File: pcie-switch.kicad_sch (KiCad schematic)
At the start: 114 parts, among them Q2 BSS138PW,115, Q3 BSS138PW,115, Q7 BSS138PW,115, Q8 BSS138PW,115, Q9 BSS138PW,115, U1 PI7C9X3G606GP, U2 NTS0302JKZ

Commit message: [#100765] Apply fixes from review
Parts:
- removed D1, D2: LED_G_0603_LG_L29K-G2J1-24-Z, antmicro-footprints:LED_0603_1608Metric_G, symbol antmicroLEDIndicationDiscrete:LED_G_0603_LG_L29K-G2J1-24-Z
- removed R68: R_5k1_0402, antmicro-footprints:R_0402_1005Metric, symbol antmicroResistors0402:R_5k1_0402
- removed TP33: TP_1mm_SMD, antmicro-footprints:TP_SMD_1mm, symbol antmicroTestPoints:TP_1mm_SMD
- added C15, C16: C_4u7_25V_0402, antmicro-footprints:C_0402_1005Metric, symbol antmicroCapacitors0402:C_4u7_25V_0402
- added C41: C_100n_0402, antmicro-footprints:C_0402_1005Metric, symbol antmicroCapacitors0402:C_100n_0402
- added D1, D2: LED_Y_0402_VLMY1500-GS08, antmicro-footprints:LED_0402_1005Metric_Y, symbol antmicroLEDIndicationDiscrete:LED_Y_0402_VLMY1500-GS08
- added J1: Tag-Connect_TC2050-IDC-NL_2x5_P1.27mm, antmicro-footprints:Tag-Connect_TC2050-IDC-NL_2x5_P1.27mm, symbol antmicroTestPoints:Tag-Connect_TC2050-IDC-NL_2x5_P1.27mm
- added R111, R116: R_5k1_0402, antmicro-footprints:R_0402_1005Metric, symbol antmicroResistors0402:R_5k1_0402
- added R113, R114, R115, R27, R33: R_0R_0402, antmicro-footprints:R_0402_1005Metric, symbol antmicroResistors0402:R_0R_0402
- added R68: R_10k_0402, antmicro-footprints:R_0402_1005Metric, symbol antmicroResistors0402:R_10k_0402
- added TP26, TP27, TP28, TP29: TP_0.75mm_SMD, antmicro-footprints:TP_SMD_0.75mm, symbol antmicroTestPoints:TP_0.75mm_SMD
- added U12: 93AA66C_SOIC, antmicro-footprints:SOIC-8_3.9x4.9x1.75mm_P1.27mm, symbol antmicroMemory:93AA66C_SOIC
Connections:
- net +0V95: now also C15.2, C16.2
- net +1V8: now also C41.1, R111.1, R116.1, R68.2, U12.8 (VCC)
- net +3V3: now also D1.2 (A), D2.2 (A), R27.2
- net CS: now also R115.2, TP26.1, U12.1 (CS); no longer U1.M11 (~{EECS})
- net GND: now also C15.1, C16.1, C41.2, J1.3, J1.5, J1.9, U12.5 (GND)
- net MISO: now also R113.1, TP29.1, U12.4 (DO); no longer U1.J12 (EEDO)
- net MOSI: now also R114.2, TP28.1, U12.3 (DI); no longer U1.L11 (EEDI)
- net SCK: now also R33.1, TP27.1, U12.2 (CLK); no longer U1.K12 (EECK)
- net TCK: now also J1.4
- net TDI: now also J1.8
- net TDO: now also J1.6
- net TMS: now also J1.2
- net ~{RESET}: now also J1.10
- net at R21.2: now also D1.1 (C)
- net at R38.2: now also D2.1 (C)
- net at U1.L12 (SCL_I2C), U2.2 (A1): now also R111.2
- net at U1.M12 (SDA_I2C), U2.3 (A2): now also R116.2
- net ~{CLKREQ1}: no longer names the net of U1.E4 (~{CLKREQ1})
- new net: J1.1, R27.1
- new net: R114.1, U1.L11 (EEDI)
- new net: R68.1, U12.6 (ORG)
- new net: R113.2, U1.J12 (EEDO)
- new net: R115.1, U1.M11 (~{EECS})
- new net: R33.2, U1.K12 (EECK)
- no-connect marks 11 -> 12
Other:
- moved on the sheet: C10, C11, C12, C13, C14, C18, C2, C20, C21, C22, C26, C27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

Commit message: [#100765] Reset designators
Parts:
- renumbered C26 to C24, C5 to C25, C27 to C26, C2 to C27, C31 to C28, C6 to C29, C28 to C30, C3 to C31, C58 to C32, C29 to C33, C30 to C34, C32 to C35, C37 to C36, C33 to C37, C34 to C38, C64 to C39, C35 to C40, C7 to C41, C18 to C42, C38 to C43, C21 to C44, C36 to C45, C39 to C46, C8 to C47, C20 to C48, C22 to C49, C15 to C50, C4 to C51, C9 to C52, C10 to C53, C11 to C54, C12 to C55, C13 to C56, C14 to C57, C16 to C58, C41 to C59, D1 to D3, D2 to D4, D8 to D5, D9 to D6, D10 to D7, J1 to J5, Q2 to Q1, Q3 to Q2, Q7 to Q3, Q8 to Q4, Q9 to Q5, R33 to R32, R113 to R33, R21 to R34, R114 to R35, R115 to R36, R38 to R37, R7 to R38, R111 to R39, R5 to R40, R65 to R41, R116 to R42, R8 to R43, R25 to R44, R26 to R45, R6 to R46, R67 to R47, R19 to R48, R18 to R49, R100 to R50, R101 to R51, R98 to R52, R99 to R53, R1 to R54, R2 to R55, R39 to R56, R40 to R57, R45 to R58, R47 to R59, R46 to R60, R48 to R61, R41 to R62, R68 to R63, R82 to R64, R112 to R65, R11 to R66, R42 to R67, R43 to R68, R9 to R69, R10 to R70, R44 to R71, R36 to R72, R27 to R73, R34 to R74, R37 to R75, R35 to R76, R49 to R77, R85 to R78, R86 to R79, R28 to R80, R29 to R81, R50 to R82, R51 to R83, TP36 to TP19, TP37 to TP20, TP31 to TP21, TP24 to TP22, TP25 to TP23, TP26 to TP24, TP28 to TP25, TP27 to TP26, TP29 to TP27, TP40 to TP28, TP5 to TP29, TP12 to TP30, TP38 to TP31, TP39 to TP32, TP13 to TP33, TP14 to TP34, TP16 to TP35, TP6 to TP36, TP7 to TP37, TP8 to TP38, TP9 to TP39, TP10 to TP40, TP11 to TP41, TP17 to TP42, TP32 to TP43, TP34 to TP44, TP35 to TP45, U1 to U4, U2 to U5, U12 to U6

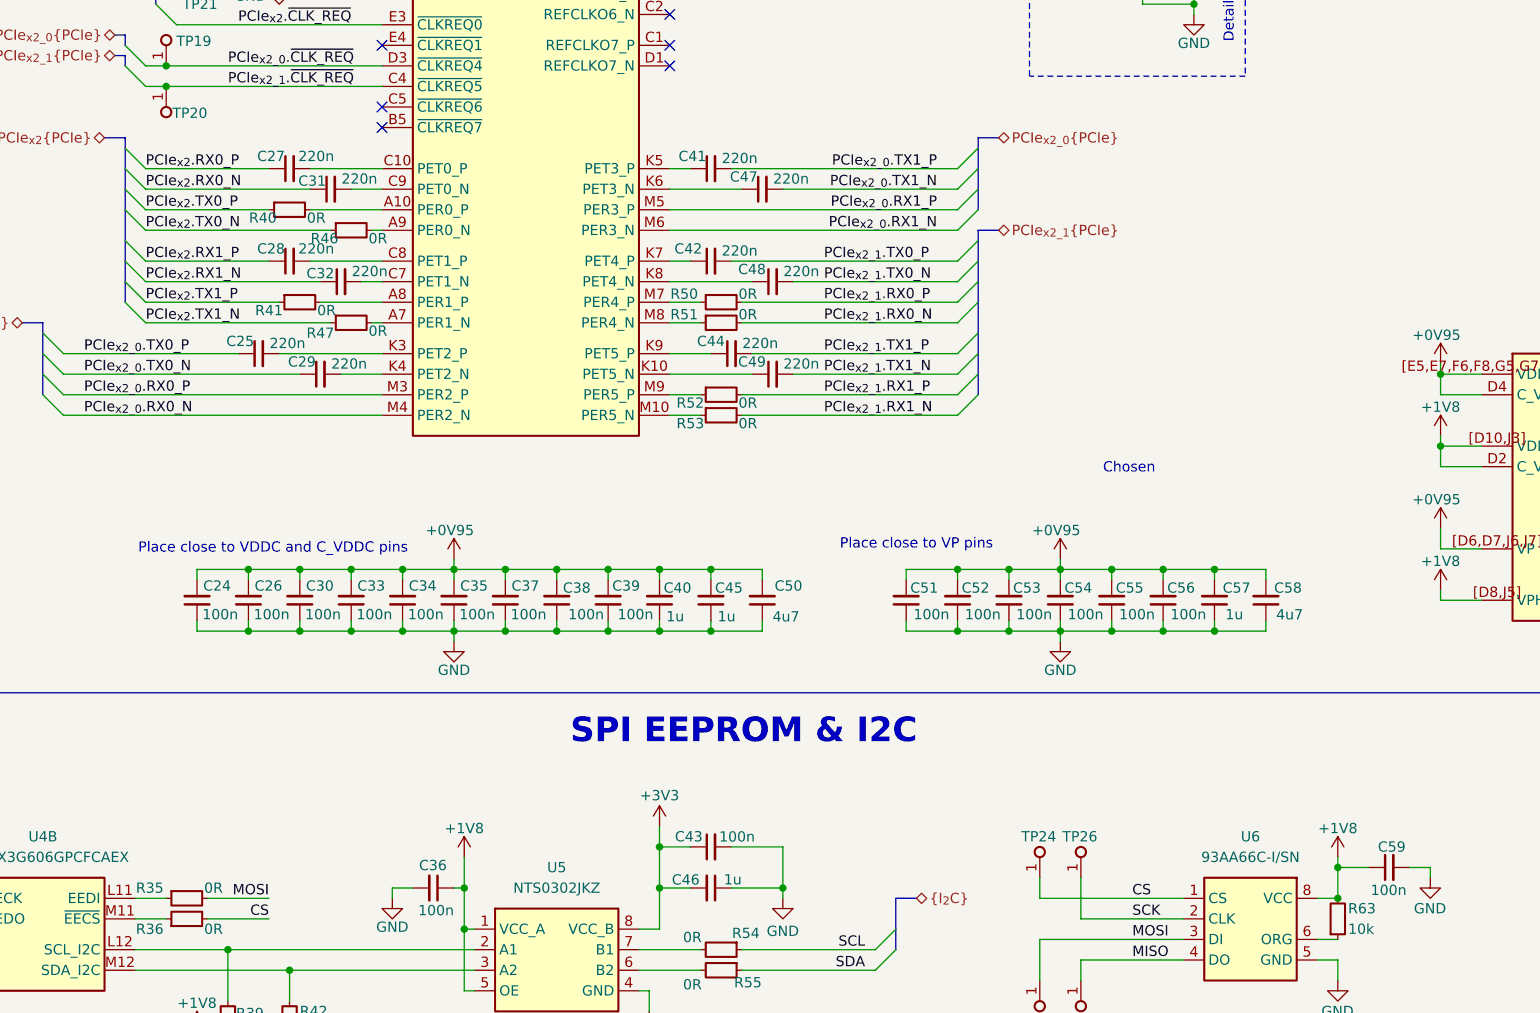
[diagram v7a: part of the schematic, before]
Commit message: [#101557] Add 0R on EEPROM VCC
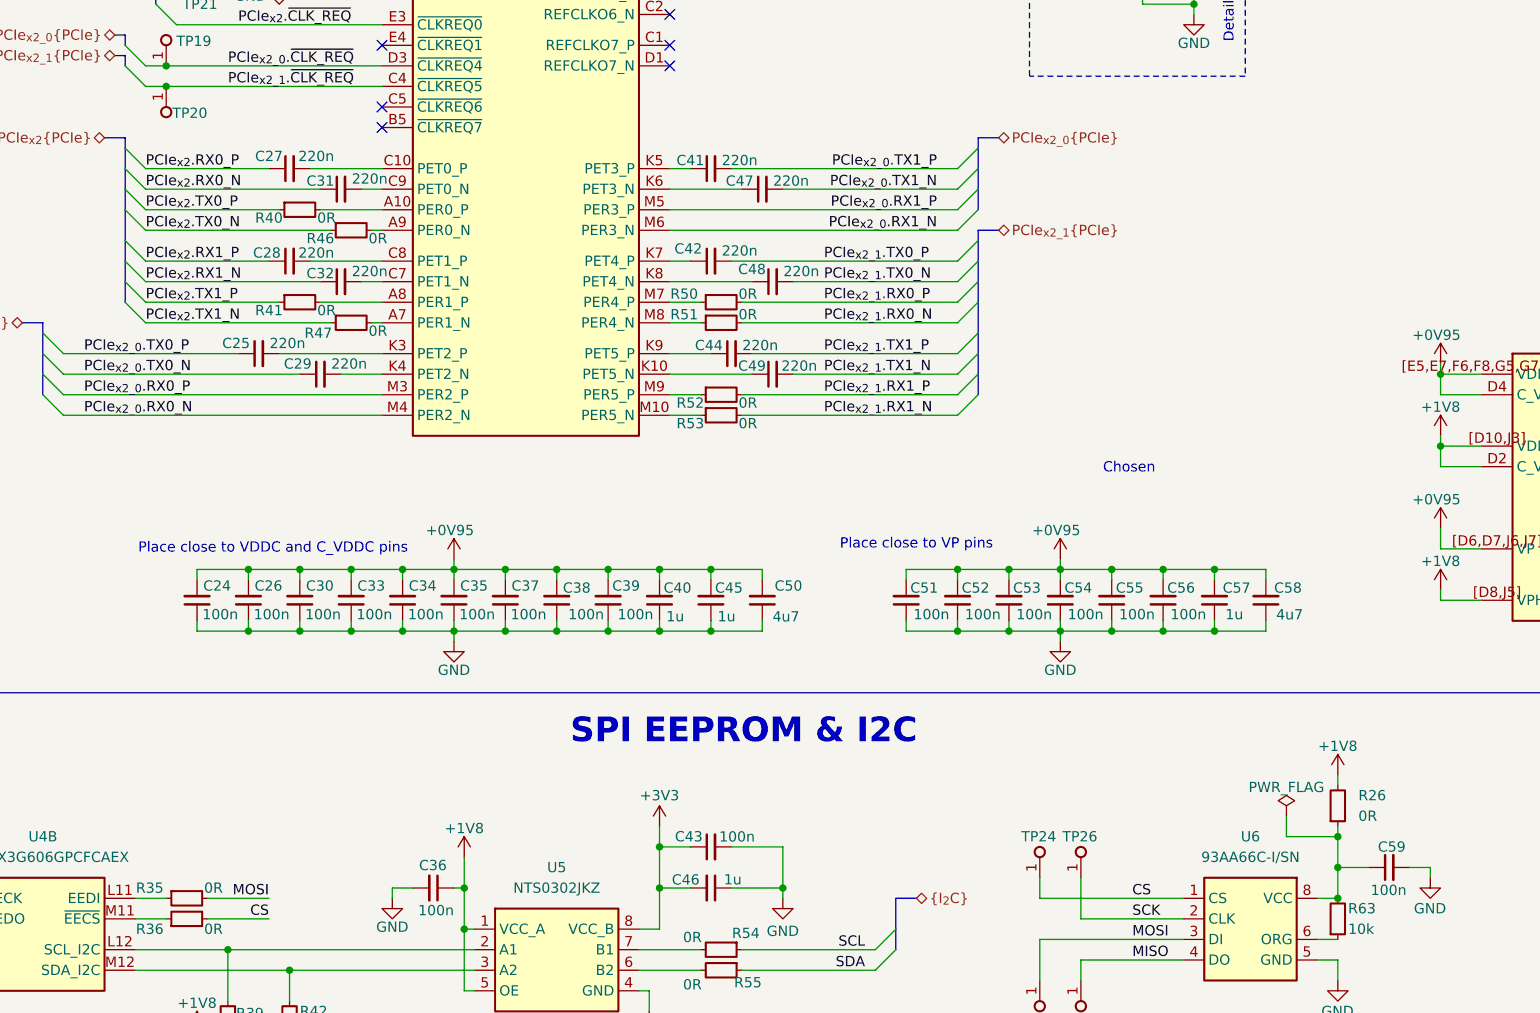
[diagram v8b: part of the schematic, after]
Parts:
- added R26: R_0R_0402, antmicro-footprints:R_0402_1005Metric, symbol antmicroResistors0402:R_0R_0402
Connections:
- net +1V8: now also R26.2; no longer C59.1, R63.2, U6.8 (VCC)
- new net: C59.1, R26.1, R63.2, U6.8 (VCC)
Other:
- moved on the sheet: C31, R40
